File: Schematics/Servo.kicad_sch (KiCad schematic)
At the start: 6 parts, among them CN1 Limit Switch Connector 1, CN2 Limit Switch Connector 2, J4 Screw_Terminal_01x02, J5 Screw_Terminal_01x02

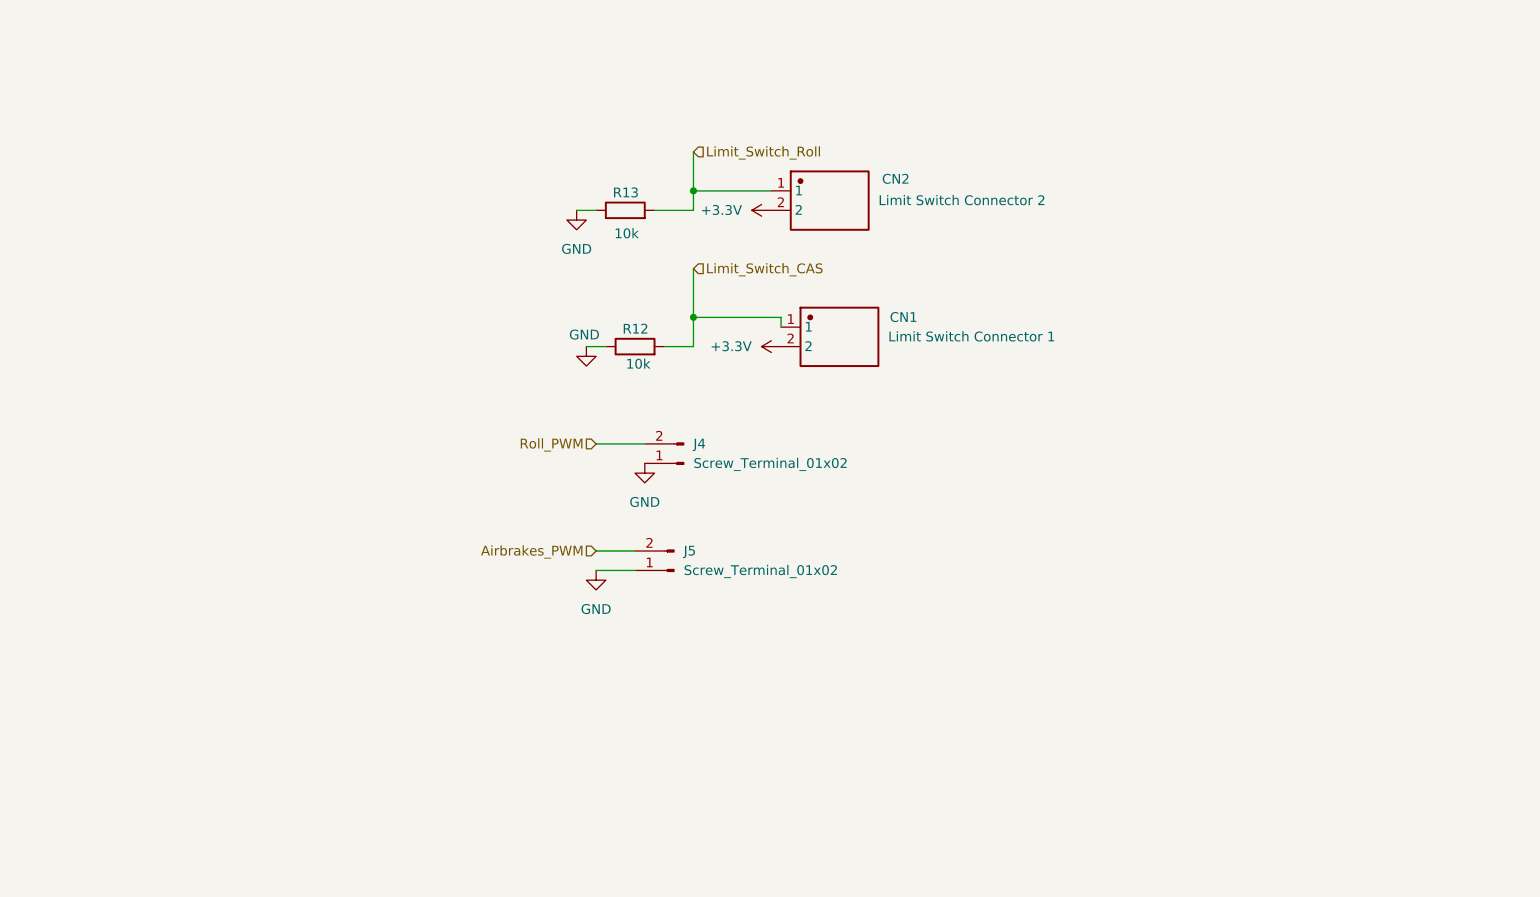
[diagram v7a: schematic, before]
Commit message: Added encoder connection for parafoil motor position information, in buy order ready for purchase
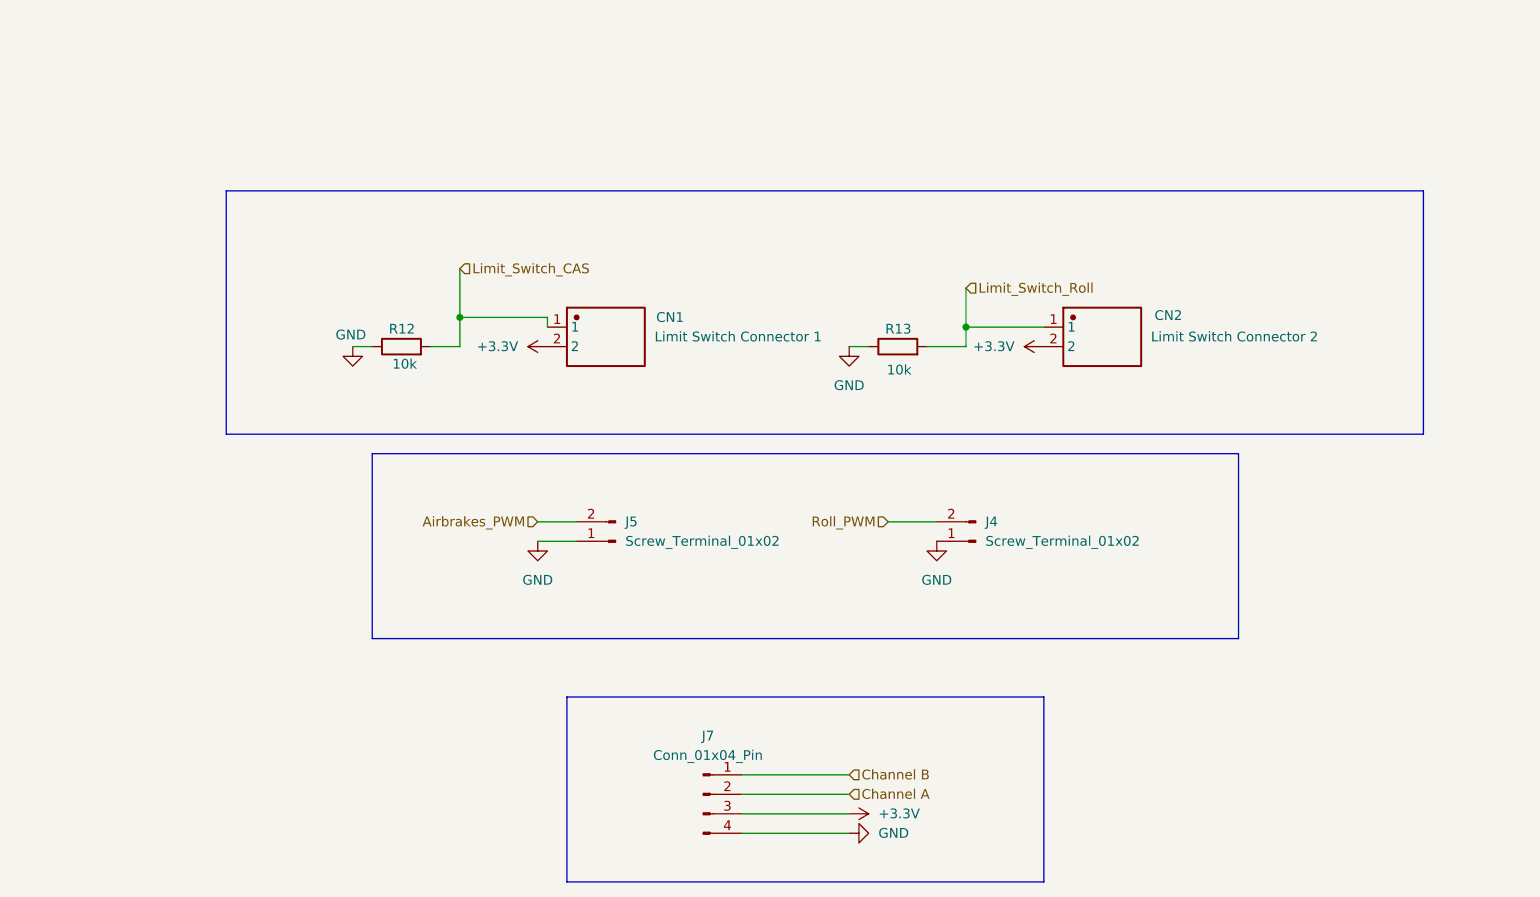
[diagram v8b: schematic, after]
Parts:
- added J7: Conn_01x04_Pin, Connector_JST:JST_PH_B4B-PH-K_1x04_P2.00mm_Vertical, symbol Connector:Conn_01x04_Pin
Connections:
- net +3.3V: now also J7.3 (Pin_3)
- net GND: now also J7.4 (Pin_4)
- new net Channel A: J7.2 (Pin_2)
- new net Channel B: J7.1 (Pin_1)
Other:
- moved on the sheet: CN1, CN2, J4, J5, R12, R13
